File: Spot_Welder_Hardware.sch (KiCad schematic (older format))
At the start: 148 parts, among them J1 Mini USB, J2 Conn_01x03_Male, Q1 Q_NMOS_GSD, Q10 Q_NMOS_GDS, Q11 Q_NMOS_GDS, Q12 Q_NMOS_GDS, Q13 Q_NMOS_GDS, Q2 2N2219, Q4 Q_NMOS_GDS, Q5 Q_NMOS_GDS, Q6 Q_NMOS_GDS, Q7 Q_NMOS_GDS, Q8 Q_NMOS_GDS, Q9 Q_NMOS_GDS, SW1 SW_Push, SW2 SW_SPDT, SW3 Lead Voltage Trigger, SW4 SW_Push, U1 OKI, U2 ATMEGA328P, U3 FAN3122TMXCT-ND, U4 FT232RL, U5 FAN3122TMXCT-ND, Y1 Crystal

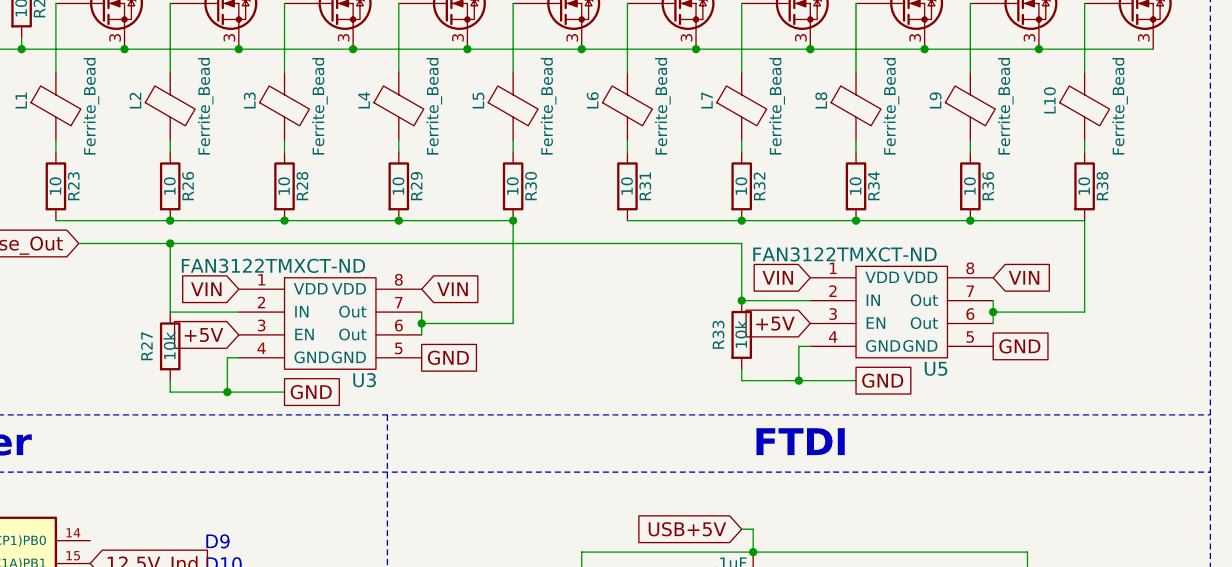
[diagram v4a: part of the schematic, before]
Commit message: Changed Gate Driver Power to V+
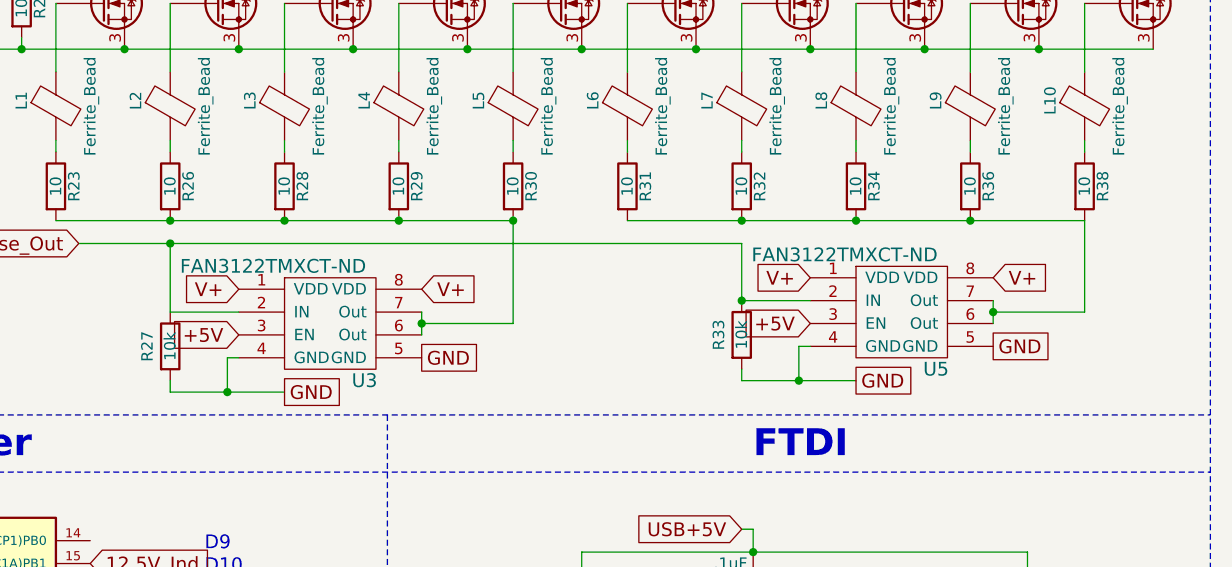
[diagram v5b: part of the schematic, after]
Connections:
- net labels removed: VIN
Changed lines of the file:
@@
 Text GLabel 9950 2250 0    60   Output ~ 0
 V+
-Text GLabel 11850 4000 2    60   Input ~ 0
-VIN
-Text GLabel 11050 4000 0    60   Input ~ 0
-VIN
 Text GLabel 11850 4300 2    60   UnSpc ~ 0
 GND
@@
 	1    0    0    -1
 $EndComp
-Text GLabel 14350 3950 2    60   Input ~ 0
-VIN
-Text GLabel 13550 3950 0    60   Input ~ 0
-VIN
 Text GLabel 14350 4250 2    60   UnSpc ~ 0
 GND
@@
 Wire Wire Line
 	5150 6950 5150 7000
+Text GLabel 11050 4000 0    60   Input ~ 0
+V+
+Text GLabel 11850 4000 2    60   Input ~ 0
+V+
+Text GLabel 13550 3950 0    60   Input ~ 0
+V+
+Text GLabel 14350 3950 2    60   Input ~ 0
+V+
 $EndSCHEMATC

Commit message: Changed BJT
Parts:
- Conn3: footprint (none) -> MRDT_Connectors:Anderson_2_Horisontal_Side_by_Side
- Q2: value 2N2219 -> MBT3904; footprint TO_SOT_Packages_THT:TO-39-3 -> TO_SOT_Packages_SMD:SOT-23
- gave numbers to parts that had none: 2
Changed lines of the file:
@@
 Text GLabel 4850 5200 0    60   UnSpc ~ 0
 Power_GND
-Text GLabel 5700 3900 2    60   Input ~ 0
+Text GLabel 5700 4100 2    60   Input ~ 0
 Conn_GND
 Text GLabel 5250 5300 2    60   Output ~ 0
@@
 P 8800 2950
 F 0 "Q2" H 8800 3100 50  0000 L CNN
-F 1 "2N2219" H 8600 2800 50  0000 L CNN
-F 2 "TO_SOT_Packages_THT:TO-39-3" H 9000 2875 50  0001 L CIN
+F 1 "MBT3904" H 8600 2800 50  0000 L CNN
+F 2 "TO_SOT_Packages_SMD:SOT-23" H 9000 2875 50  0001 L CIN
 F 3 "" H 8800 2950 50  0001 L CNN
 	1    8800 2950
@@
 	0    1    1    0
 $EndComp
-Text GLabel 5700 3600 2    60   Output ~ 0
+Text GLabel 5700 3800 2    60   Output ~ 0
 V+
 Wire Notes Line
@@
 L MRDT_Connectors:AndersonPP Conn3
 U 1 1 5BB3DDFC
-P 5300 4000
-F 0 "Conn3" H 5506 4387 60  0000 C CNN
-F 1 "AndersonPP" H 5506 4281 60  0000 C CNN
-F 2 "" H 5150 3450 60  0001 C CNN
-F 3 "" H 5150 3450 60  0001 C CNN
-	1    5300 4000
-	1    0    0    -1
-$EndComp
-$Comp
-L MRDT_Connectors:AndersonPP Conn3
-U 2 1 5BB3DF96
-P 5300 3700
-F 0 "Conn3" H 5506 4087 60  0000 C CNN
-F 1 "AndersonPP" H 5506 3981 60  0000 C CNN
-F 2 "" H 5150 3150 60  0001 C CNN
-F 3 "" H 5150 3150 60  0001 C CNN
-	2    5300 3700
+P 5300 4200
+F 0 "Conn3" H 5506 4587 60  0000 C CNN
+F 1 "AndersonPP" H 5506 4481 60  0000 C CNN
+F 2 "MRDT_Connectors:Anderson_2_Horisontal_Side_by_Side" H 5150 3650 60  0001 C CNN
+F 3 "" H 5150 3650 60  0001 C CNN
+	1    5300 4200
 	1    0    0    -1
 $EndComp
@@
 $EndComp
 $Comp
-L Device:Q_NMOS_GDS Q?
+L Device:Q_NMOS_GDS Q3
 U 1 1 5BBA9147
 P 9200 2950
-F 0 "Q?" H 9400 3000 50  0000 L CNN
+F 0 "Q3" H 9400 3000 50  0000 L CNN
 F 1 "Q_NMOS_GDS" H 9400 2900 50  0001 L CNN
 F 2 "TO_SOT_Packages_THT:TO-220-3_Vertical" H 9400 3050 50  0001 C CNN
@@
 	6550 6700 6500 6700
 $Comp
-L Device:D_Zener D?
+L Device:D_Zener D8
 U 1 1 5BC50F38
 P 4750 6700
-F 0 "D?" H 4750 6800 50  0000 C CNN
+F 0 "D8" H 4750 6800 50  0000 C CNN
 F 1 "5V" H 4750 6600 50  0000 C CNN
 F 2 "Diodes_SMD:D_SOD-123" H 4750 6700 50  0001 C CNN
@@
 Text GLabel 14350 3950 2    60   Input ~ 0
 V+
+$Comp
+L MRDT_Connectors:AndersonPP Conn3
+U 2 1 5BB3DF96
+P 5300 3900
+F 0 "Conn3" H 5506 4287 60  0000 C CNN
+F 1 "AndersonPP" H 5506 4181 60  0000 C CNN
+F 2 "MRDT_Connectors:Anderson_2_Horisontal_Side_by_Side" H 5150 3350 60  0001 C CNN
+F 3 "" H 5150 3350 60  0001 C CNN
+	2    5300 3900
+	1    0    0    -1
+$EndComp
 $EndSCHEMATC

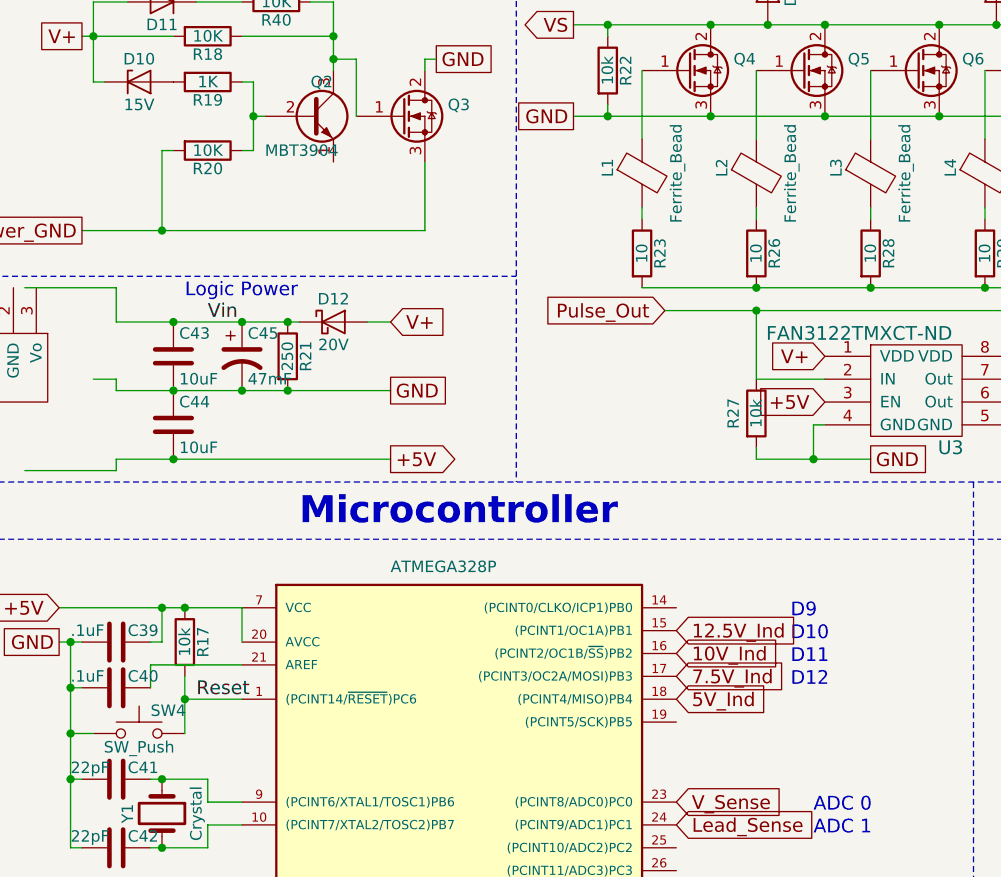
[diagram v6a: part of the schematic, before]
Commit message: Re-routed LED indications in ATMEGA
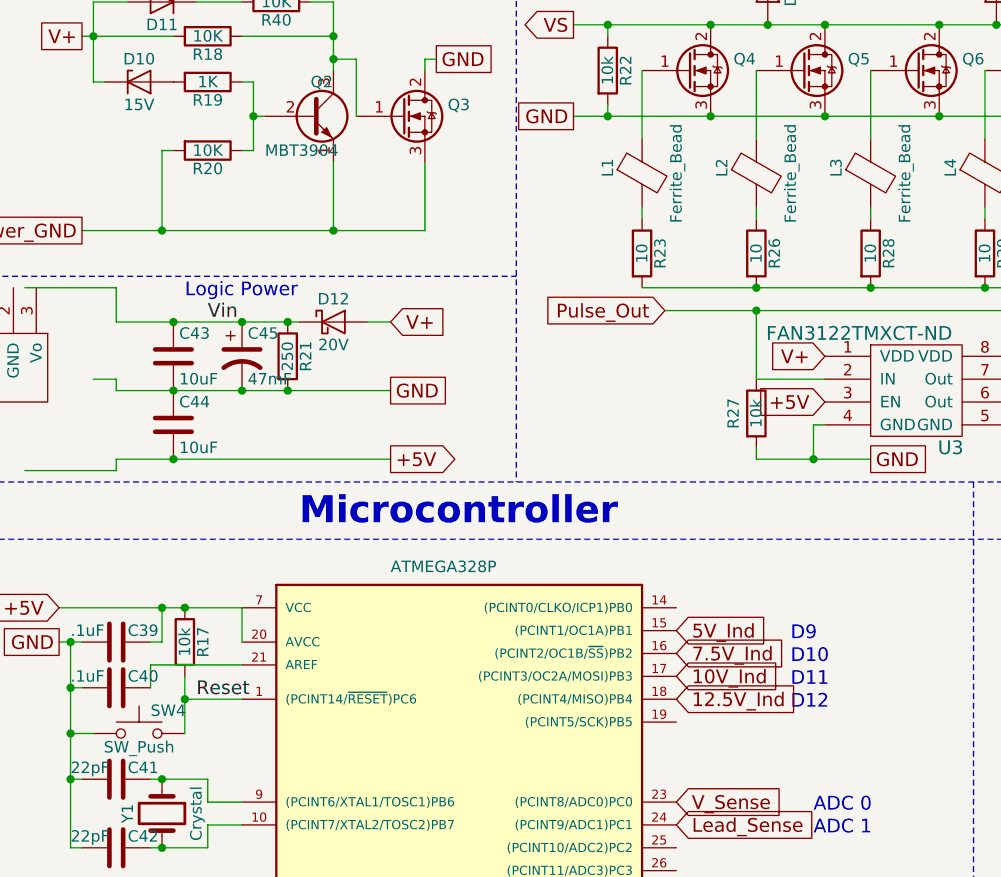
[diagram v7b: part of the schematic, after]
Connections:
- wire segments 324 -> 326
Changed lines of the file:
@@
 Text Notes 6750 5900 0    20   ~ 0
 Used to toggle\nlead voltage trigger mode
+Text GLabel 10400 5200 2    60   Input ~ 0
+5V_Ind
+Text GLabel 10400 5300 2    60   Input ~ 0
+7.5V_Ind
+Text GLabel 10400 5400 2    60   Input ~ 0
+10V_Ind
 Text GLabel 10400 5500 2    60   Input ~ 0
-5V_Ind
-Text GLabel 10400 5400 2    60   Input ~ 0
-7.5V_Ind
-Text GLabel 10400 5300 2    60   Input ~ 0
-10V_Ind
-Text GLabel 10400 5200 2    60   Input ~ 0
 12.5V_Ind
+Text Notes 10900 5550 0    60   ~ 0
+D12
 Text Notes 10900 5450 0    60   ~ 0
-D12
+D11
 Text Notes 10900 5350 0    60   ~ 0
-D11
+D10
 Text Notes 10900 5250 0    60   ~ 0
-D10
-Text Notes 10900 5150 0    60   ~ 0
 D9
 Text GLabel 10400 7300 2    60   Input ~ 0
@@
 	8900 2450 8800 2450
 Wire Wire Line
-	8150 3450 9300 3450
+	8150 3450 8900 3450
 Connection ~ 8900 2600
 Wire Wire Line
@@
 	1    0    0    -1
 $EndComp
+Wire Wire Line
+	8900 3150 8900 3450
+Connection ~ 8900 3450
+Wire Wire Line
+	8900 3450 9300 3450
 $EndSCHEMATC

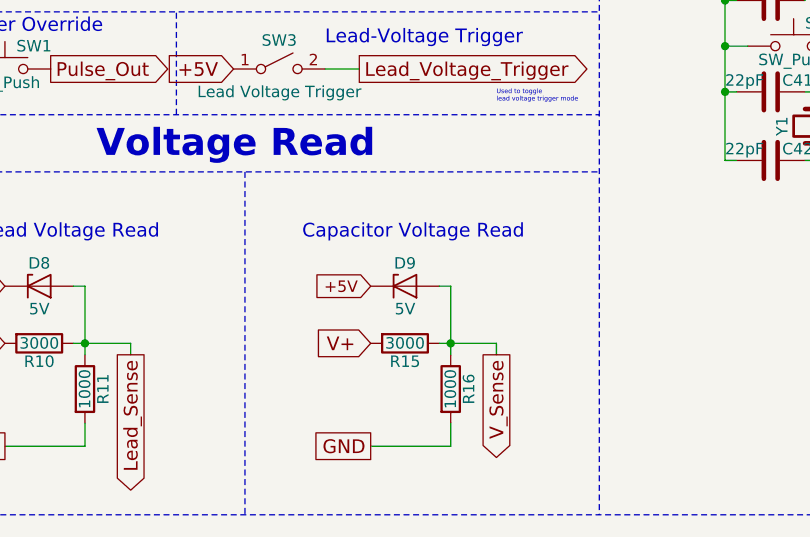
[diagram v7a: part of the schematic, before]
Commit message: Replaced D8, D9 with Shottky Diode
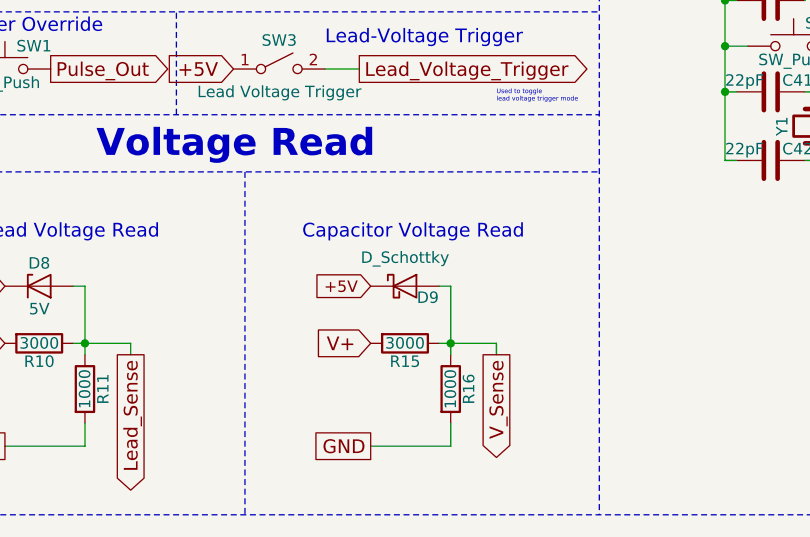
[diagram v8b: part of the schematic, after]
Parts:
- removed D9: 5V, Diodes_SMD:D_SOD-123, symbol Device:D_Zener
- added D9: D_Schottky, Diode_SMD:D_0603_1608Metric_Pad1.05x0.95mm_HandSolder, symbol Device:D_Schottky
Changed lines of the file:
@@
 Text GLabel 6750 7000 3    60   Output ~ 0
 V_Sense
-$Comp
-L Device:D_Zener D9
-U 1 1 5B33E128
-P 6350 6700
-F 0 "D9" H 6350 6800 50  0000 C CNN
-F 1 "5V" H 6350 6600 50  0000 C CNN
-F 2 "Diodes_SMD:D_SOD-123" H 6350 6700 50  0001 C CNN
-F 3 "" H 6350 6700 50  0001 C CNN
-F 4 "BZT52C5V1-FDICT-ND" H 6350 6700 60  0001 C CNN "Part Number"
-	1    6350 6700
-	1    0    0    -1
-$EndComp
 Text GLabel 2250 6200 0    60   Input ~ 0
 5V_Ind
@@
 Wire Wire Line
 	8900 3450 9300 3450
+$Comp
+L Device:D_Schottky D9
+U 1 1 5BB3740A
+P 6350 6700
+F 0 "D9" H 6450 6650 50  0000 C CNN
+F 1 "D_Schottky" H 6350 6825 50  0000 C CNN
+F 2 "Diode_SMD:D_0603_1608Metric_Pad1.05x0.95mm_HandSolder" H 6350 6700 50  0001 C CNN
+F 3 "~" H 6350 6700 50  0001 C CNN
+	1    6350 6700
+	1    0    0    -1
+$EndComp
 $EndSCHEMATC
